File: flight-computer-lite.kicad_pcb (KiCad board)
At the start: 2 copper layers, 65 x 65 mm, 85 parts, among them J1 USB_C_Receptacle_USB2.0_16P, J2 Micro_SD_Card_Det2, J3 Conn_01x02_Pin, J4 Conn_01x03_Pin, Q1 BSS138, SW1 SW_Push, SW2 SW_Push, U1 RP2040, U10 SAM-M10Q, U11 LM66200DRLR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

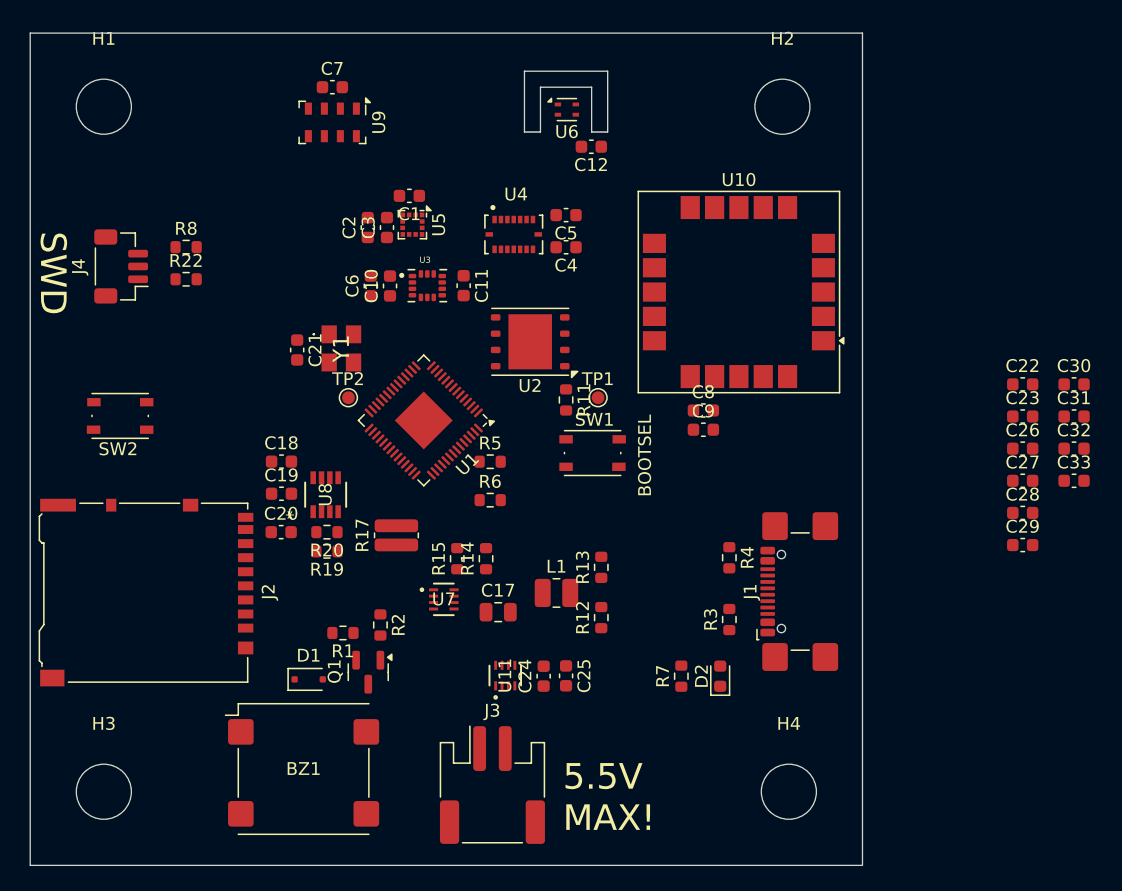
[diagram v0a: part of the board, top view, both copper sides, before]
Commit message: Added more 3d models and rearranged layout
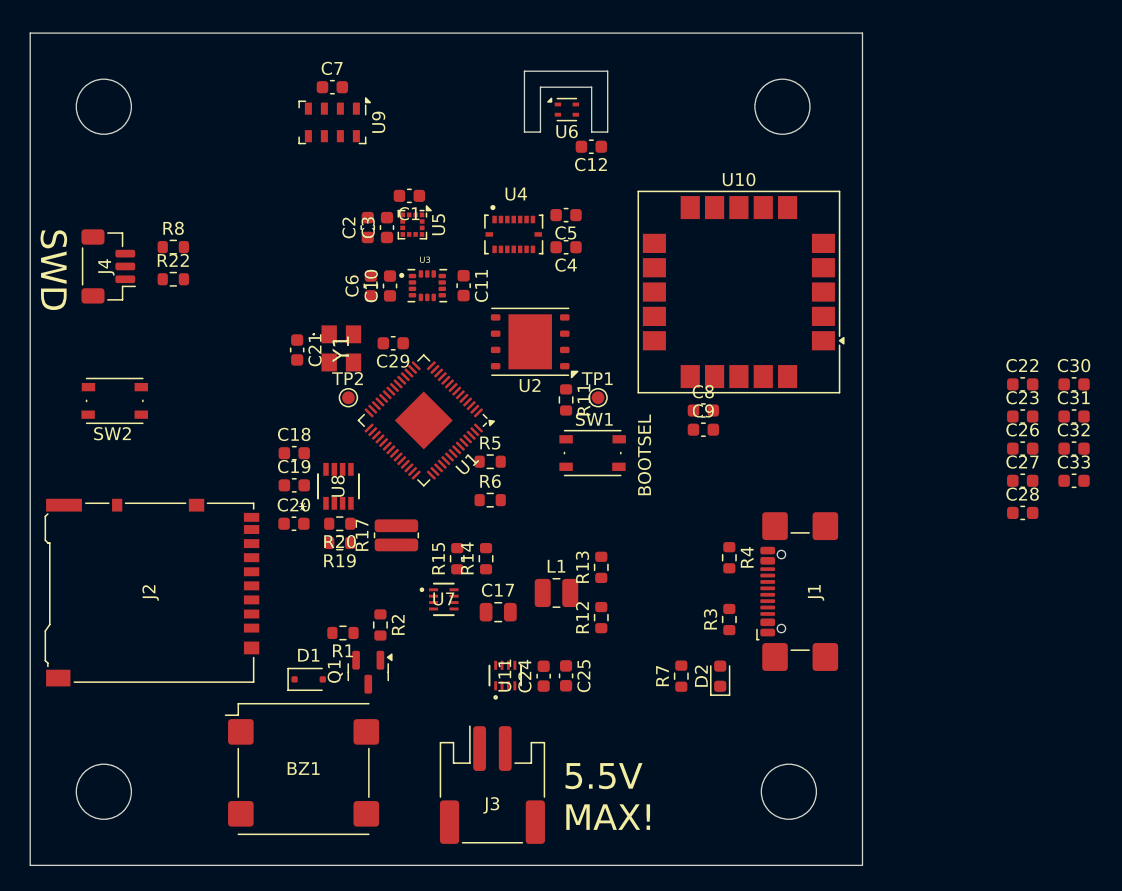
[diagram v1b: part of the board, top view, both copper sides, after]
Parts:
- moved C29 51.6 mm to (154.5, 79.5), turned to 180 degrees
- moved SW2 1.25 mm to (132.8, 84.0)
- moved C19 1.20 mm to (146.8, 90.6)
- moved C20 1.20 mm to (146.8, 93.6)
- moved R19 1.20 mm to (150.3, 95.1)
- moved R20 1.20 mm to (150.3, 93.6)
- moved U8 1.20 mm to (150.2, 90.7)
- moved C18 1.20 mm to (146.8, 88.1)
- moved J4 1.00 mm to (132.2, 73.5)
- moved R22 1.00 mm to (137.3, 74.5)
- moved R8 1.00 mm to (137.3, 72.0)
- moved J2 0.47 mm to (135.7, 99.0)
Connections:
- U1 pad 15: /USR -> unconnected-(U1-GPIO12-Pad15)
- U1 pad 16: unconnected-(U1-GPIO13-Pad16) -> /USR

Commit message: WIP layout/route
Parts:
- removed C8: 1u, Capacitor_SMD:C_0603_1608Metric
- removed C9: 0.1u, Capacitor_SMD:C_0603_1608Metric
- removed U10: SAM-M10Q, RF_GPS:ublox_SAM-M8Q
- added AE1: Antenna, Connector_Coaxial:U.FL_Hirose_U.FL-R-SMT-1_Vertical, F.Cu at (166.5, 110.0)
- added C34: 0.1u, Capacitor_SMD:C_0603_1608Metric, F.Cu at (150.9, 108.5)
- added C35: 1u, Capacitor_SMD:C_0603_1608Metric, F.Cu at (151.0, 110.0)
- added D3: LED, LED_SMD:LED_0603_1608Metric, F.Cu at (143.6, 86.5)
- added R23: R, Resistor_SMD:R_0603_1608Metric, F.Cu at (140.4, 86.5)
- added TP3: TestPoint, TestPoint:TestPoint_Pad_D1.0mm, F.Cu at (187.8, 102.4)
- added U12: MAX-M10S, LRI_partlib:ublox_MAX, F.Cu at (158.5, 106.5)
- C30, C31: value 2.2u -> 1u
- R10, R18, R21, R9: value I2C -> 1k
- moved R18 159.3 mm to (90.2, 90.5)
- moved R21 159.2 mm to (90.2, 93.0)
- moved C14 145.3 mm to (100.8, 71.9)
- moved C15 145.2 mm to (100.8, 74.5)
- moved C16 144.2 mm to (100.8, 77.0)
- moved R16 144.1 mm to (108.8, 71.9)
- moved R9 138.5 mm to (104.8, 56.1)
- moved R10 138.4 mm to (104.8, 58.6)
- moved C13 85.6 mm to (153.9, 73.0), turned to 90 degrees
- moved C25 70.4 mm to (104.8, 74.5), turned to 0 degrees
- moved R12 70.1 mm to (104.8, 77.0), turned to 0 degrees
- moved C24 70.0 mm to (104.8, 71.9), turned to 0 degrees
- moved R13 68.2 mm to (104.8, 79.5), turned to 0 degrees
- moved L1 61.7 mm to (106.6, 87.6)
- moved R14 58.7 mm to (104.8, 82.0), turned to 0 degrees
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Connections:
- net /PSU/ST renamed /PSU/POR_ST
- J2 pad 1: unconnected-(J2-DAT2-Pad1) -> /DAT2
- J2 pad 10: /SD_DET -> /CARD_DET
- J2 pad 2: unconnected-(J2-DAT3/CD-Pad2) -> /DAT3/CS
- J2 pad 3: unconnected-(J2-CMD-Pad3) -> /CMD/MOSI
- J2 pad 5: unconnected-(J2-CLK-Pad5) -> /SD_CLK
- J2 pad 7: unconnected-(J2-DAT0-Pad7) -> /DAT0/MISO
- J2 pad 8: unconnected-(J2-DAT1-Pad8) -> /DAT1
- SW2 pad 1: /USR -> /USR_BTN
- U1 pad 13: unconnected-(U1-GPIO10-Pad13) -> /I2C Bus 2/I2C_2_SDA
- U1 pad 14: unconnected-(U1-GPIO11-Pad14) -> /I2C Bus 2/I2C_2_SCL
- U1 pad 16: /USR -> unconnected-(U1-GPIO13-Pad16)
- U1 pad 2: /I2C_1_SDA -> /I2C Bus 1/I2C_1_SDA
- U1 pad 28: unconnected-(U1-GPIO17-Pad28) -> /CARD_DET
- U1 pad 29: unconnected-(U1-GPIO18-Pad29) -> /SD_CLK
- U1 pad 3: /I2C_1_SCL -> /I2C Bus 1/I2C_1_SCL
- U1 pad 30: unconnected-(U1-GPIO19-Pad30) -> /CMD/MOSI
- U1 pad 31: unconnected-(U1-GPIO20-Pad31) -> /DAT0/MISO
- U1 pad 32: unconnected-(U1-GPIO21-Pad32) -> /DAT1
- U1 pad 34: unconnected-(U1-GPIO22-Pad34) -> /DAT2
- U1 pad 35: unconnected-(U1-GPIO23-Pad35) -> /DAT3/CS
- U1 pad 4: /I2C Bus 2/I2C_2_SDA -> unconnected-(U1-GPIO2-Pad4)
- U1 pad 43: unconnected-(U1-ADC_AVDD-Pad43) -> +3V3
- U1 pad 45: +3V3 -> +1V1
- U1 pad 5: /I2C Bus 2/I2C_2_SCL -> unconnected-(U1-GPIO3-Pad5)
- U1 pad 7: unconnected-(U1-GPIO5-Pad7) -> /BUZZER_CTL
- U1 pad 8: unconnected-(U1-GPIO6-Pad8) -> /USR_LED
- U1 pad 9: unconnected-(U1-GPIO7-Pad9) -> /USR_BTN
- U5 pad 1: /I2C Bus 1/I2C_1_SCL -> /I2C Bus 2/I2C_2_SCL
- U5 pad 11: /I2C Bus 1/I2C_1_SDA -> /I2C Bus 2/I2C_2_SDA
- U8 pad 5: /PSU/I2C_1_SCL -> /I2C Bus 1/I2C_1_SCL
- U8 pad 6: /PSU/I2C_1_SDA -> /I2C Bus 1/I2C_1_SDA
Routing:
- net +3V3: track 0.00 -> 78.5 mm
- net GND: track 0.00 -> 66.1 mm, vias 0 -> 47
- net /I2C Bus 2/I2C_2_SDA: track 0.00 -> 62.7 mm
- net /I2C Bus 2/I2C_2_SCL: track 0.00 -> 50.8 mm
- net /CARD_DET: track 0.00 -> 37.2 mm
- net /I2C Bus 1/I2C_1_SCL: track 0.00 -> 28.6 mm
- net /DAT1: track 0.00 -> 24.9 mm, vias 0 -> 2
- net /DAT3/CS: track 0.00 -> 22.6 mm
- net /DAT0/MISO: track 0.00 -> 22.2 mm, vias 0 -> 2
- net /I2C Bus 1/I2C_1_SDA: track 0.00 -> 21.2 mm
- net /CPU_USB_D-: track 0.00 -> 20.9 mm
- net /CPU_USB_D+: track 0.00 -> 20.9 mm
- net /SD_CLK: track 0.00 -> 18.6 mm
- net /DAT2: track 0.00 -> 18.0 mm
- net /CMD/MOSI: track 0.00 -> 17.8 mm
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- added copper zone on B.Cu, net GND
- added copper zone on F.Cu, net GND
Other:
- outline, holes or cut-outs redrawn
- rule pad_to_mask_clearance: 0 -> 0.0508
- board text removed: "5.5V MAX!"
- board text removed: "BOOTSEL"
- board text removed: "SWD"

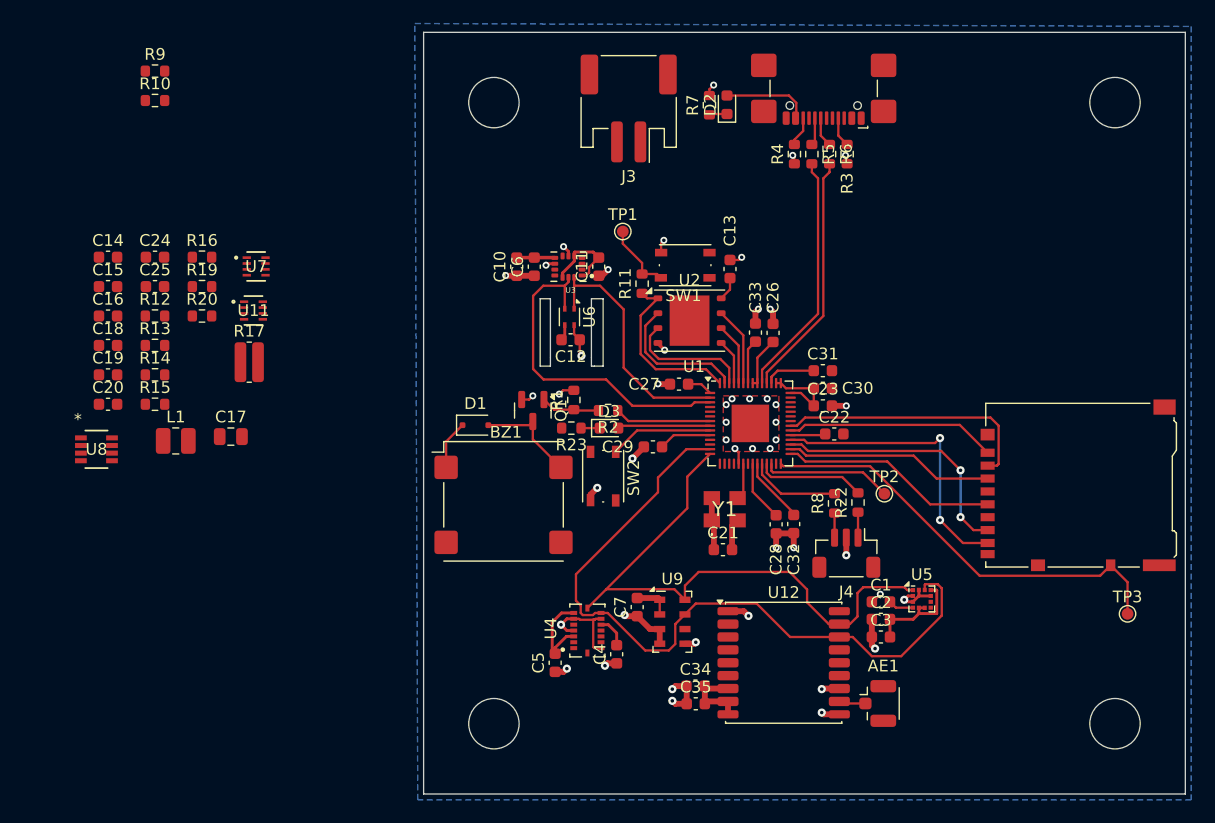
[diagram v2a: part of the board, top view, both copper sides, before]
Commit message: Routed PSU
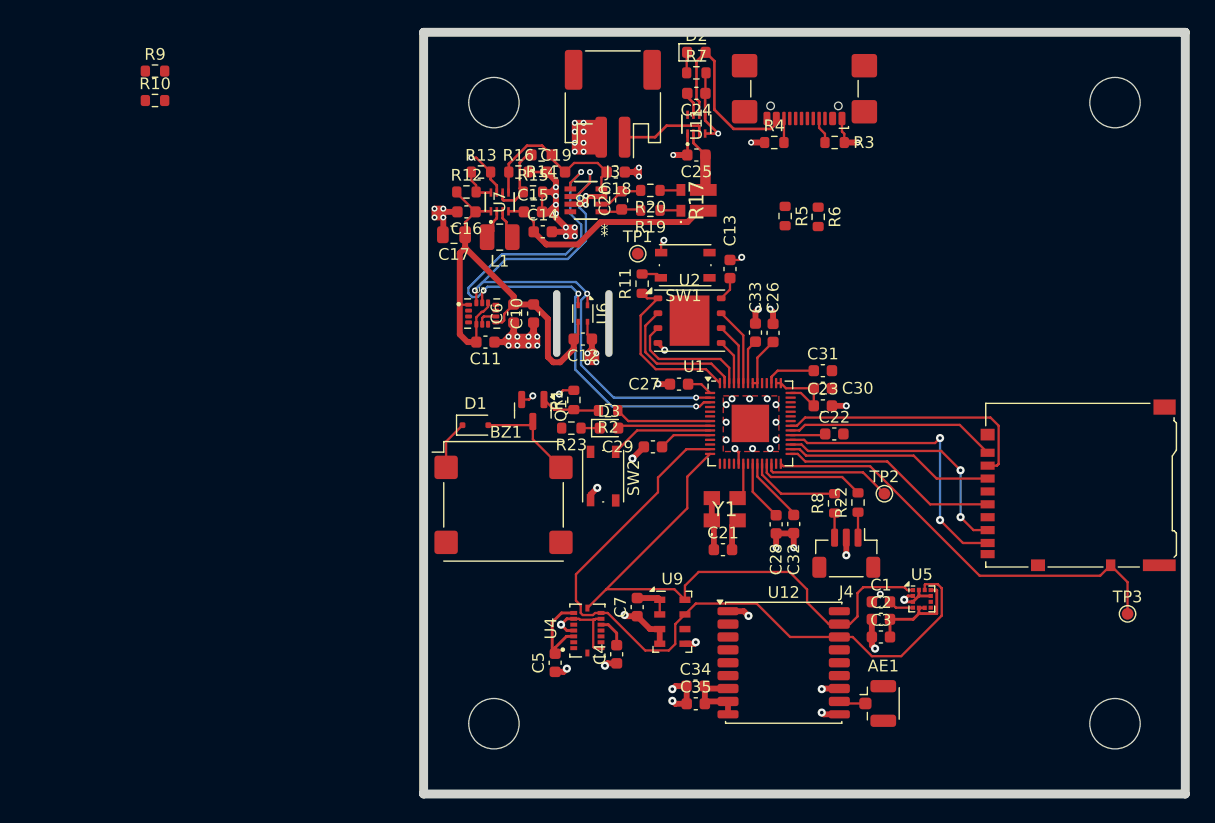
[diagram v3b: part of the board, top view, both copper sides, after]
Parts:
- R17: footprint Resistor_SMD:R_0612_1632Metric -> LRI_partlib:L4CA0612L0M50FNR
- moved C24 48.3 mm to (151.0, 58.0), turned to 180 degrees
- moved C25 47.5 mm to (151.0, 63.2), turned to 180 degrees
- moved C20 47.2 mm to (144.7, 67.1), turned to 90 degrees
- moved U8 46.9 mm to (141.6, 67.1), turned to 180 degrees
- moved C18 45.8 mm to (144.1, 64.7), turned to 180 degrees
- moved C19 42.0 mm to (139.0, 64.7)
- moved U11 41.0 mm to (151.0, 60.6), turned to 90 degrees
- moved R17 40.6 mm to (151.0, 67.1), turned to 90 degrees
- moved R20 39.7 mm to (147.1, 66.2), turned to 180 degrees
- moved R19 38.8 mm to (147.1, 67.9), turned to 180 degrees
- moved R14 38.0 mm to (137.8, 63.2), turned to 180 degrees
- moved C14 37.2 mm to (137.9, 69.8)
- moved R15 37.0 mm to (137.1, 66.4)
- moved C15 36.8 mm to (137.1, 68.1)
- moved L1 32.7 mm to (134.2, 70.2), turned to 180 degrees
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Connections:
- R17 pad 1: /PSU/+IN -> /PSU/-SNS
- R19 pad 1: /PSU/+IN -> /PSU/-SNS
- R20 pad 1: /PSU/-IN -> /PSU/+SNS
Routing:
- net GND: track 66.1 -> 111.4 mm, vias 47 -> 80
- net +3V3: track 78.5 -> 111.8 mm
- net /I2C Bus 1/I2C_1_SDA: track 21.2 -> 51.8 mm, vias 0 -> 4
- net /I2C Bus 1/I2C_1_SCL: track 28.6 -> 51.9 mm, vias 0 -> 4
- net /PSU/+IN: track 0.00 -> 22.2 mm
- net /CPU_USB_D-: track 20.9 -> 0.00 mm
- net /CPU_USB_D+: track 20.9 -> 0.00 mm
- net /PSU/-IN: track 0.00 -> 19.5 mm
- net VBUS: track 7.50 -> 17.5 mm
- net +BATT: track 0.00 -> 7.41 mm
- net Net-(U7-MODE): track 0.00 -> 6.63 mm
- net /BOOTSEL: track 6.04 -> 1.73 mm
- net Net-(U8-IN-): track 0.00 -> 3.84 mm
- net Net-(U8-IN+): track 0.00 -> 3.47 mm
- net /PSU/TPS_FB: track 0.00 -> 3.15 mm
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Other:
- outline, holes or cut-outs redrawn

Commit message: major routing update!
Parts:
- R10, R11, R18, R21, R9: value 1k -> 1K
- R16: value 10k -> 10K
- U5: footprint Package_LGA:LGA-12_2x2mm_P0.5mm -> LRI_partlib:LGA-12_2x2mm_P0.5mm
- U8: value INA232AIDDFR -> SOT_32AIDDFR_TEX
- moved R9 59.3 mm to (148.9, 95.8)
- moved R10 55.4 mm to (147.3, 94.1), turned to 180 degrees
- moved J1 33.6 mm to (188.6, 74.5), turned to 90 degrees
- moved R4 26.1 mm to (181.9, 71.8), turned to -90 degrees
- moved R3 25.0 mm to (182.8, 77.1), turned to 90 degrees
- moved J3 16.3 mm to (160.2, 58.4)
- moved R6 11.0 mm to (163.7, 79.3), turned to 180 degrees
- moved R5 10.2 mm to (163.8, 77.2), turned to 180 degrees
- moved C1 5.25 mm to (172.0, 101.0), turned to -90 degrees
- moved C2 4.17 mm to (170.5, 101.0), turned to -90 degrees
- moved C3 4.02 mm to (169.0, 101.0), turned to -90 degrees
- moved U5 3.94 mm to (172.3, 104.5), turned to -90 degrees
- moved C29 1.66 mm to (148.9, 87.8)
- moved C4 1.53 mm to (144.3, 104.3)
- moved C5 1.30 mm to (139.1, 105.2)
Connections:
- AE1 pad 2: (no net) -> GND
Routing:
- net VBUS: track 17.5 -> 26.0 mm, vias 0 -> 2
- net /I2C Bus 2/I2C_2_SDA: track 62.7 -> 54.9 mm, vias 0 -> 4
- net GND: track 111.4 -> 118.0 mm, vias 80 -> 89
- net /USB_D+: track 0.00 -> 5.42 mm
- net +3V3: track 111.8 -> 117.2 mm, vias 0 -> 2
- net /USB_D-: track 0.00 -> 4.57 mm
- net /I2C Bus 2/I2C_2_SCL: track 50.8 -> 53.0 mm, vias 0 -> 4
- net /DAT3/CS: track 22.6 -> 23.9 mm
- net Net-(J1-CC2): track 2.05 -> 3.03 mm
- net /DAT1: track 24.9 -> 24.3 mm
